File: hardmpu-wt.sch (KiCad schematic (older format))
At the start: 39 parts, among them J1 MIDI, J2 User, J4 ISP, J5 JTAG, J8 XT Bus, U1 74HCT138, U2 74HCT138, U3 74HCT08, U4 74HCT574, U5 74HCT574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

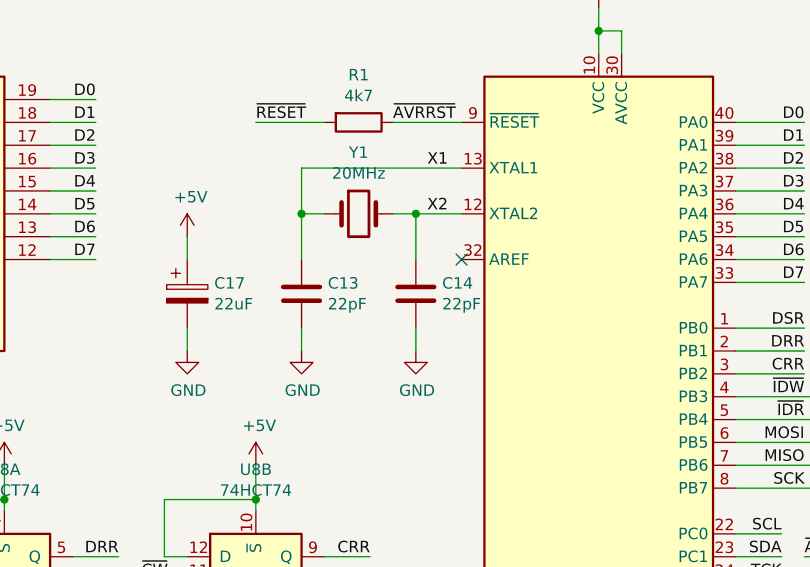
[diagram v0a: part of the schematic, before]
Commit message: Tweak component values
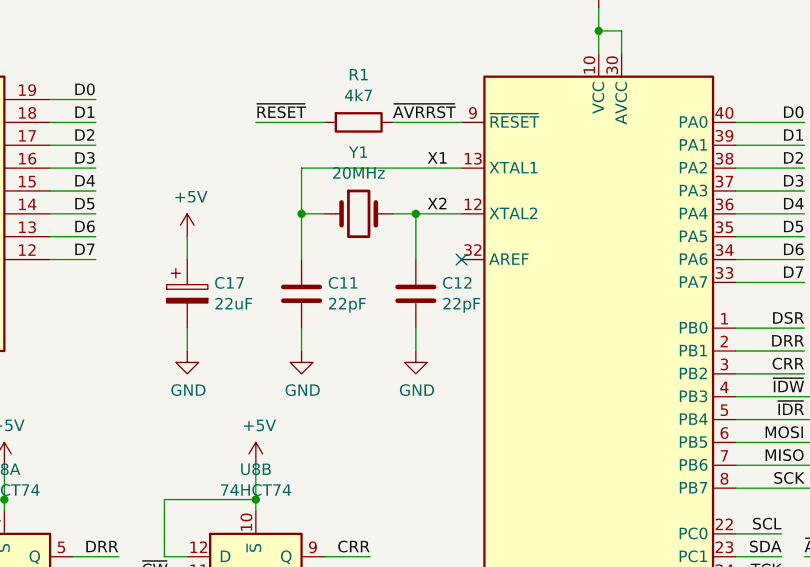
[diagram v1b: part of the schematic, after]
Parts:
- renumbered C13 to C11, C14 to C12
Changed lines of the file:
@@
 	6400 1700 6500 1700
 $Comp
-L Device:C C13
+L Device:C C11
 U 1 1 624D3BFD
 P 6400 2050
-F 0 "C13" H 6515 2096 50  0000 L CNN
+F 0 "C11" H 6515 2096 50  0000 L CNN
 F 1 "22pF" H 6515 2005 50  0000 L CNN
 F 2 "Capacitor_THT:C_Disc_D3.0mm_W1.6mm_P2.50mm" H 6438 1900 50  0001 C CNN
@@
 $EndComp
 $Comp
-L Device:C C14
+L Device:C C12
 U 1 1 624D4044
 P 6900 2050
-F 0 "C14" H 7015 2096 50  0000 L CNN
+F 0 "C12" H 7015 2096 50  0000 L CNN
 F 1 "22pF" H 7015 2005 50  0000 L CNN
 F 2 "Capacitor_THT:C_Disc_D3.0mm_W1.6mm_P2.50mm" H 6938 1900 50  0001 C CNN

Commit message: Move DA-15 so board aligns with Keystone 9200-11 bracket
Adapt board to fit common Keystone 9200-11, add jumpers to switch wavetable between Internal and External UART
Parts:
- added JP3: WT Port, Connector_PinHeader_2.54mm:PinHeader_2x03_P2.54mm_Vertical, symbol Connector_Generic:Conn_02x03_Odd_Even
- H1: value WT_Hole1 -> WT_Hole
- H2: value WT_Hole2 -> WT_Hole
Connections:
- net labels added: RX0, RX1, TX0, TX1, WT_RX, WT_TX
- net labels removed: MIDI_RX, MIDI_TX, USER4, USER5
- wire segments 371 -> 377
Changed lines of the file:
@@
 Wire Wire Line
 	8300 3200 8500 3200
-Text Label 8600 4200 2    50   ~ 0
-USER0
-Text Label 8600 4300 2    50   ~ 0
-USER1
-Text Label 8600 4400 2    50   ~ 0
-USER2
-Text Label 8600 4500 2    50   ~ 0
-USER3
-Text Label 8600 4600 2    50   ~ 0
-USER4
-Text Label 8600 4700 2    50   ~ 0
-USER5
 $Comp
 L Device:R R3
@@
 Wire Wire Line
 	9450 6000 9850 6000
-Text Label 8850 5400 0    50   ~ 0
-MIDI_TX
-Text Label 8850 6000 0    50   ~ 0
-MIDI_RX
-Wire Wire Line
-	8850 6000 9150 6000
-Wire Wire Line
-	8850 5400 9150 5400
+Wire Wire Line
+	8950 6000 9150 6000
+Wire Wire Line
+	8950 5400 9150 5400
 Text Label 9450 5400 0    50   ~ 0
 TX'
@@
 F1 "wavetable.sch" 50
 $EndSheet
-Text GLabel 8400 4100 2    50   Output ~ 0
-MIDI_TX
-Text GLabel 8400 4000 2    50   Input ~ 0
-MIDI_RX
 $Comp
 L Connector:Bus_ISA_8bit J8
@@
 Text GLabel 2650 6700 2    50   Output ~ 0
 ~RESET
-Wire Wire Line
-	8300 4000 8400 4000
-Wire Wire Line
-	8300 4100 8400 4100
 $Comp
 L Mechanical:MountingHole H1
@@
 P 6400 5000
 F 0 "H1" H 6500 5046 50  0000 L CNN
-F 1 "WT_Hole1" H 6500 4955 50  0000 L CNN
+F 1 "WT_Hole" H 6500 4955 50  0000 L CNN
 F 2 "MountingHole:MountingHole_3.2mm_M3" H 6400 5000 50  0001 C CNN
 F 3 "~" H 6400 5000 50  0001 C CNN
@@
 P 6400 5200
 F 0 "H2" H 6500 5246 50  0000 L CNN
-F 1 "WT_Hole2" H 6500 5155 50  0000 L CNN
+F 1 "WT_Hole" H 6500 5155 50  0000 L CNN
 F 2 "MountingHole:MountingHole_3.2mm_M3" H 6400 5200 50  0001 C CNN
 F 3 "~" H 6400 5200 50  0001 C CNN
@@
 $EndComp
 NoConn ~ 6400 5550
+Text Label 8600 4400 2    50   ~ 0
+USER0
+Text Label 8600 4500 2    50   ~ 0
+USER1
+Text Label 8600 4600 2    50   ~ 0
+USER2
+Text Label 8600 4700 2    50   ~ 0
+USER3
+Wire Wire Line
+	8300 4100 8600 4100
+Wire Wire Line
+	8300 4000 8600 4000
+Text Label 8600 4200 2    50   ~ 0
+RX1
+Text Label 8600 4300 2    50   ~ 0
+TX1
+Text Label 8600 4000 2    50   ~ 0
+RX0
+Text Label 8600 4100 2    50   ~ 0
+TX0
+Text Label 8950 5400 0    50   ~ 0
+TX0
+Text Label 8950 6000 0    50   ~ 0
+RX0
+$Comp
+L Connector_Generic:Conn_02x03_Odd_Even JP3
+U 1 1 62929CB7
+P 9400 1400
+F 0 "JP3" H 9450 1717 50  0000 C CNN
+F 1 "WT Port" H 9450 1626 50  0000 C CNN
+F 2 "Connector_PinHeader_2.54mm:PinHeader_2x03_P2.54mm_Vertical" H 9400 1400 50  0001 C CNN
+F 3 "~" H 9400 1400 50  0001 C CNN
+	1    9400 1400
+	1    0    0    -1
+$EndComp
+Text GLabel 9100 1400 0    50   Input ~ 0
+WT_RX
+Text GLabel 9800 1400 2    50   Output ~ 0
+WT_TX
+Wire Wire Line
+	9100 1400 9200 1400
+Wire Wire Line
+	9700 1400 9800 1400
+Wire Wire Line
+	9200 1300 9000 1300
+Wire Wire Line
+	9200 1500 9000 1500
+Wire Wire Line
+	9700 1300 9900 1300
+Wire Wire Line
+	9700 1500 9900 1500
+Text Label 9000 1500 0    50   ~ 0
+RX0
+Text Label 9000 1300 0    50   ~ 0
+RX1
+Text Label 9900 1500 2    50   ~ 0
+TX0
+Text Label 9900 1300 2    50   ~ 0
+TX1
 $EndSCHEMATC
